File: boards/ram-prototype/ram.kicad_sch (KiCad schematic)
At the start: 47 parts, among them J1 SRAM_Bus, J2 Probe, J3 Unused_COL_SEL

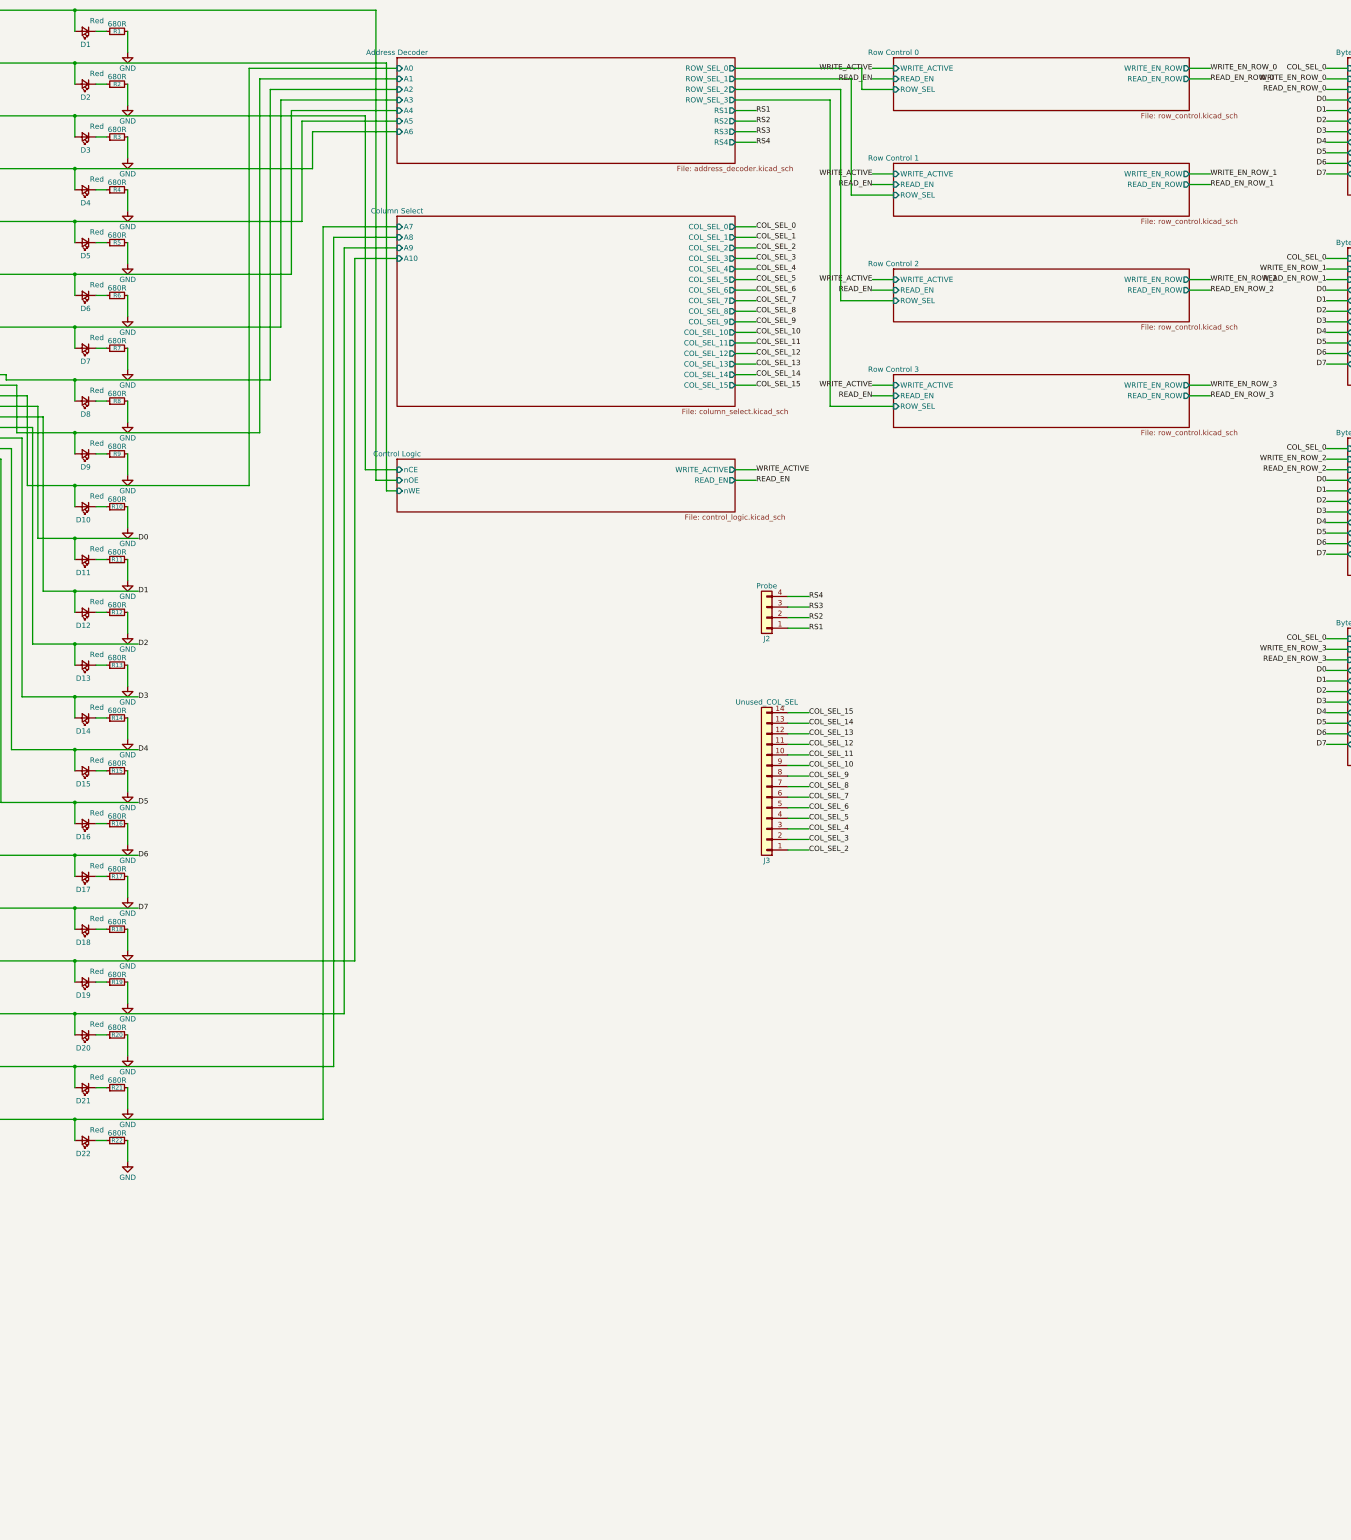
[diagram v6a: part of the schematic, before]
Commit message: Update row select to have the full complexity to test latency
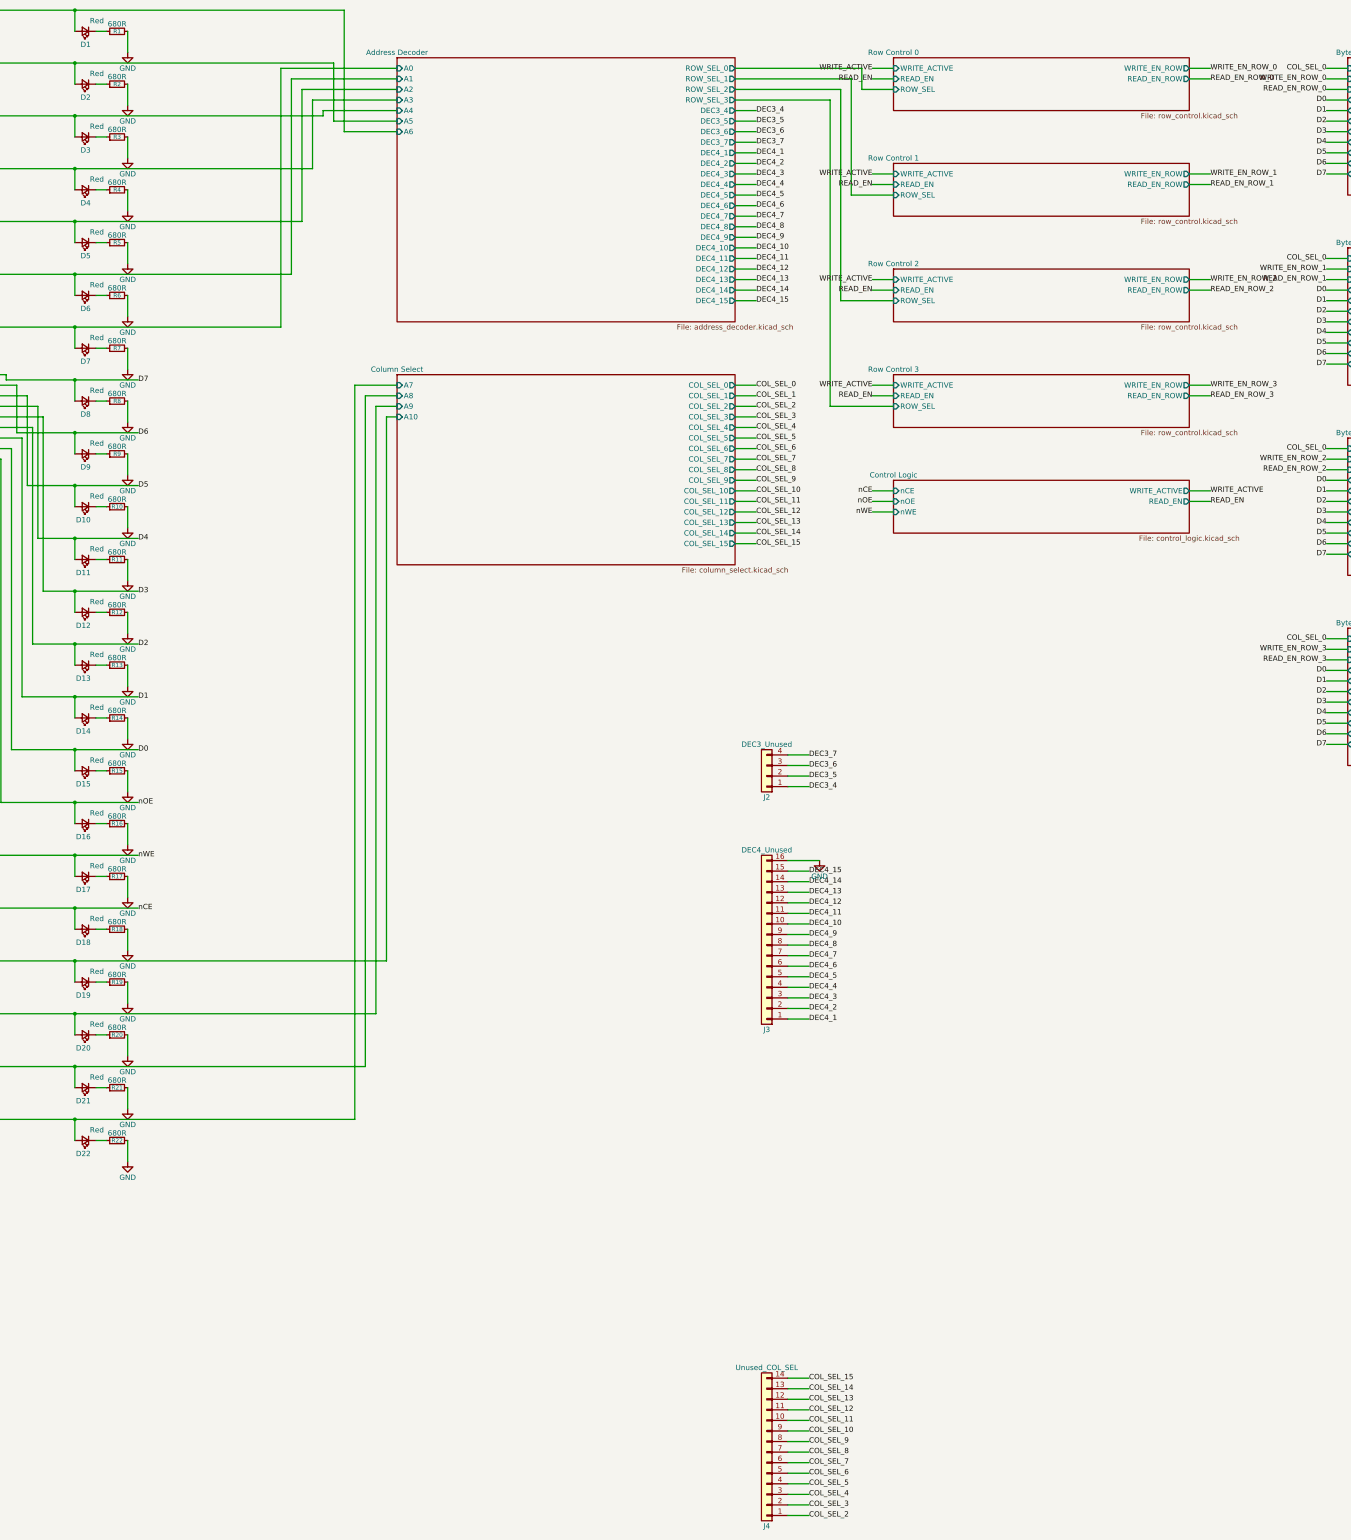
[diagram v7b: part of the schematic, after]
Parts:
- removed J3: Unused_COL_SEL, symbol Connector_Generic:Conn_01x14
- added J3: DEC4_Unused, symbol Connector_Generic:Conn_01x16
- added J4: Unused_COL_SEL, symbol Connector_Generic:Conn_01x14
- J2: value Probe -> DEC3_Unused
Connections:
- net Control Logic/nCE is gone; now on net Address Decoder/A4: D3.2 (A), J1.21 (Pin_21)
- net Control Logic/nOE is gone; now on net Address Decoder/A6: D1.2 (A), J1.23 (Pin_23)
- net Control Logic/nWE is gone; now on net Address Decoder/A5: D2.2 (A), J1.22 (Pin_22)
- net Address Decoder/A0: now also D7.2 (A), J1.17 (Pin_17); no longer D10.2 (A), J1.14 (Pin_14)
- net Address Decoder/A1: now also D6.2 (A), J1.18 (Pin_18); no longer D9.2 (A), J1.15 (Pin_15)
- net Address Decoder/A2: now also D5.2 (A), J1.19 (Pin_19); no longer D8.2 (A), J1.16 (Pin_16)
- net Address Decoder/A3: now also D4.2 (A), J1.20 (Pin_20); no longer D7.2 (A), J1.17 (Pin_17)
- net Address Decoder/A4: no longer D6.2 (A), J1.18 (Pin_18)
- net Address Decoder/A5: no longer D5.2 (A), J1.19 (Pin_19)
- net Address Decoder/A6: no longer D4.2 (A), J1.20 (Pin_20)
- net COL_SEL_10: now also J4.9 (Pin_9)
- net COL_SEL_11: now also J4.10 (Pin_10)
- net COL_SEL_12: now also J4.11 (Pin_11)
- net COL_SEL_13: now also J4.12 (Pin_12)
- net COL_SEL_14: now also J4.13 (Pin_13)
- net COL_SEL_15: now also J4.14 (Pin_14)
- net COL_SEL_2: now also J4.1 (Pin_1)
- net COL_SEL_3: now also J4.2 (Pin_2)
- net COL_SEL_4: now also J4.3 (Pin_3)
- net COL_SEL_5: now also J4.4 (Pin_4)
- net COL_SEL_6: now also J4.5 (Pin_5)
- net COL_SEL_7: now also J4.6 (Pin_6)
- net COL_SEL_8: now also J4.7 (Pin_7)
- net COL_SEL_9: now also J4.8 (Pin_8)
- net D0: now also D15.2 (A), J1.9 (Pin_9); no longer D11.2 (A), J1.13 (Pin_13)
- net D1: now also D14.2 (A), J1.10 (Pin_10); no longer D12.2 (A), J1.12 (Pin_12)
- net D3: now also D12.2 (A), J1.12 (Pin_12); no longer D14.2 (A), J1.10 (Pin_10)
- net D4: now also D11.2 (A), J1.13 (Pin_13); no longer D15.2 (A), J1.9 (Pin_9)
- net D5: now also D10.2 (A), J1.14 (Pin_14); no longer D16.2 (A), J1.8 (Pin_8)
- net D6: now also D9.2 (A), J1.15 (Pin_15); no longer D17.2 (A), J1.7 (Pin_7)
- net D7: now also D8.2 (A), J1.16 (Pin_16); no longer D18.2 (A), J1.6 (Pin_6)
- net GND: now also J3.16 (Pin_16)
- net RS1 renamed DEC3_4
- net RS2 renamed DEC3_5
- net RS3 renamed DEC3_6
- net RS4 renamed DEC3_7
- new net DEC4_1: J3.1 (Pin_1)
- new net DEC4_10: J3.10 (Pin_10)
- new net DEC4_11: J3.11 (Pin_11)
- new net DEC4_12: J3.12 (Pin_12)
- new net DEC4_13: J3.13 (Pin_13)
- new net DEC4_14: J3.14 (Pin_14)
- new net DEC4_15: J3.15 (Pin_15)
- new net DEC4_2: J3.2 (Pin_2)
- new net DEC4_3: J3.3 (Pin_3)
- new net DEC4_4: J3.4 (Pin_4)
- new net DEC4_5: J3.5 (Pin_5)
- new net DEC4_6: J3.6 (Pin_6)
- new net DEC4_7: J3.7 (Pin_7)
- new net DEC4_8: J3.8 (Pin_8)
- new net DEC4_9: J3.9 (Pin_9)
- new net nCE: D18.2 (A), J1.6 (Pin_6)
- new net nOE: D16.2 (A), J1.8 (Pin_8)
- new net nWE: D17.2 (A), J1.7 (Pin_7)
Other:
- sheet Address Decoder ports: added DEC3_4, DEC3_5, DEC3_6, DEC3_7, DEC4_1, DEC4_10, DEC4_11, DEC4_12, DEC4_13, DEC4_14, DEC4_15, DEC4_2, DEC4_3, DEC4_4, DEC4_5, DEC4_6, DEC4_7, DEC4_8, DEC4_9; removed RS1, RS2, RS3, RS4

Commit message: Fix a bunch of issues
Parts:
- removed J3: DEC4_Unused, symbol Connector_Generic:Conn_01x16
- removed J4: Unused_COL_SEL, symbol Connector_Generic:Conn_01x14
- added J3: Unused_COL_SEL, symbol Connector_Generic:Conn_01x14
- added J4: DEC4_Unused, symbol Connector_Generic:Conn_01x16
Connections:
- net COL_SEL_10: now also J3.9 (Pin_9)
- net COL_SEL_11: now also J3.10 (Pin_10)
- net COL_SEL_12: now also J3.11 (Pin_11)
- net COL_SEL_13: now also J3.12 (Pin_12)
- net COL_SEL_14: now also J3.13 (Pin_13)
- net COL_SEL_15: now also J3.14 (Pin_14)
- net COL_SEL_2: now also J3.1 (Pin_1)
- net COL_SEL_3: now also J3.2 (Pin_2)
- net COL_SEL_4: now also J3.3 (Pin_3)
- net COL_SEL_5: now also J3.4 (Pin_4)
- net COL_SEL_6: now also J3.5 (Pin_5)
- net COL_SEL_7: now also J3.6 (Pin_6)
- net COL_SEL_8: now also J3.7 (Pin_7)
- net COL_SEL_9: now also J3.8 (Pin_8)
- net DEC4_1: now also J4.1 (Pin_1)
- net DEC4_10: now also J4.10 (Pin_10)
- net DEC4_11: now also J4.11 (Pin_11)
- net DEC4_12: now also J4.12 (Pin_12)
- net DEC4_13: now also J4.13 (Pin_13)
- net DEC4_14: now also J4.14 (Pin_14)
- net DEC4_15: now also J4.15 (Pin_15)
- net DEC4_2: now also J4.2 (Pin_2)
- net DEC4_3: now also J4.3 (Pin_3)
- net DEC4_4: now also J4.4 (Pin_4)
- net DEC4_5: now also J4.5 (Pin_5)
- net DEC4_6: now also J4.6 (Pin_6)
- net DEC4_7: now also J4.7 (Pin_7)
- net DEC4_8: now also J4.8 (Pin_8)
- net DEC4_9: now also J4.9 (Pin_9)
- net GND: now also J4.16 (Pin_16)
